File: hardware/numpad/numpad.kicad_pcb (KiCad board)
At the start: 2 copper layers, 83 x 124 mm, 116 parts, among them J1 USB_C_Receptacle_USB2.0_16P, J2 Conn_01x03, J3 Conn_01x04, Q1 BSS138, Q2 BSS138, SW1 BOOTSEL, SW2 RESET, SW3 RotaryEncoder_Switch, U1 NCP1117-3.3_SOT223, U2 USBLC6-2SC6, U3 RP2040, U4 W25Q128JVS, U5 74AHCT1G125, Y1 12MHz

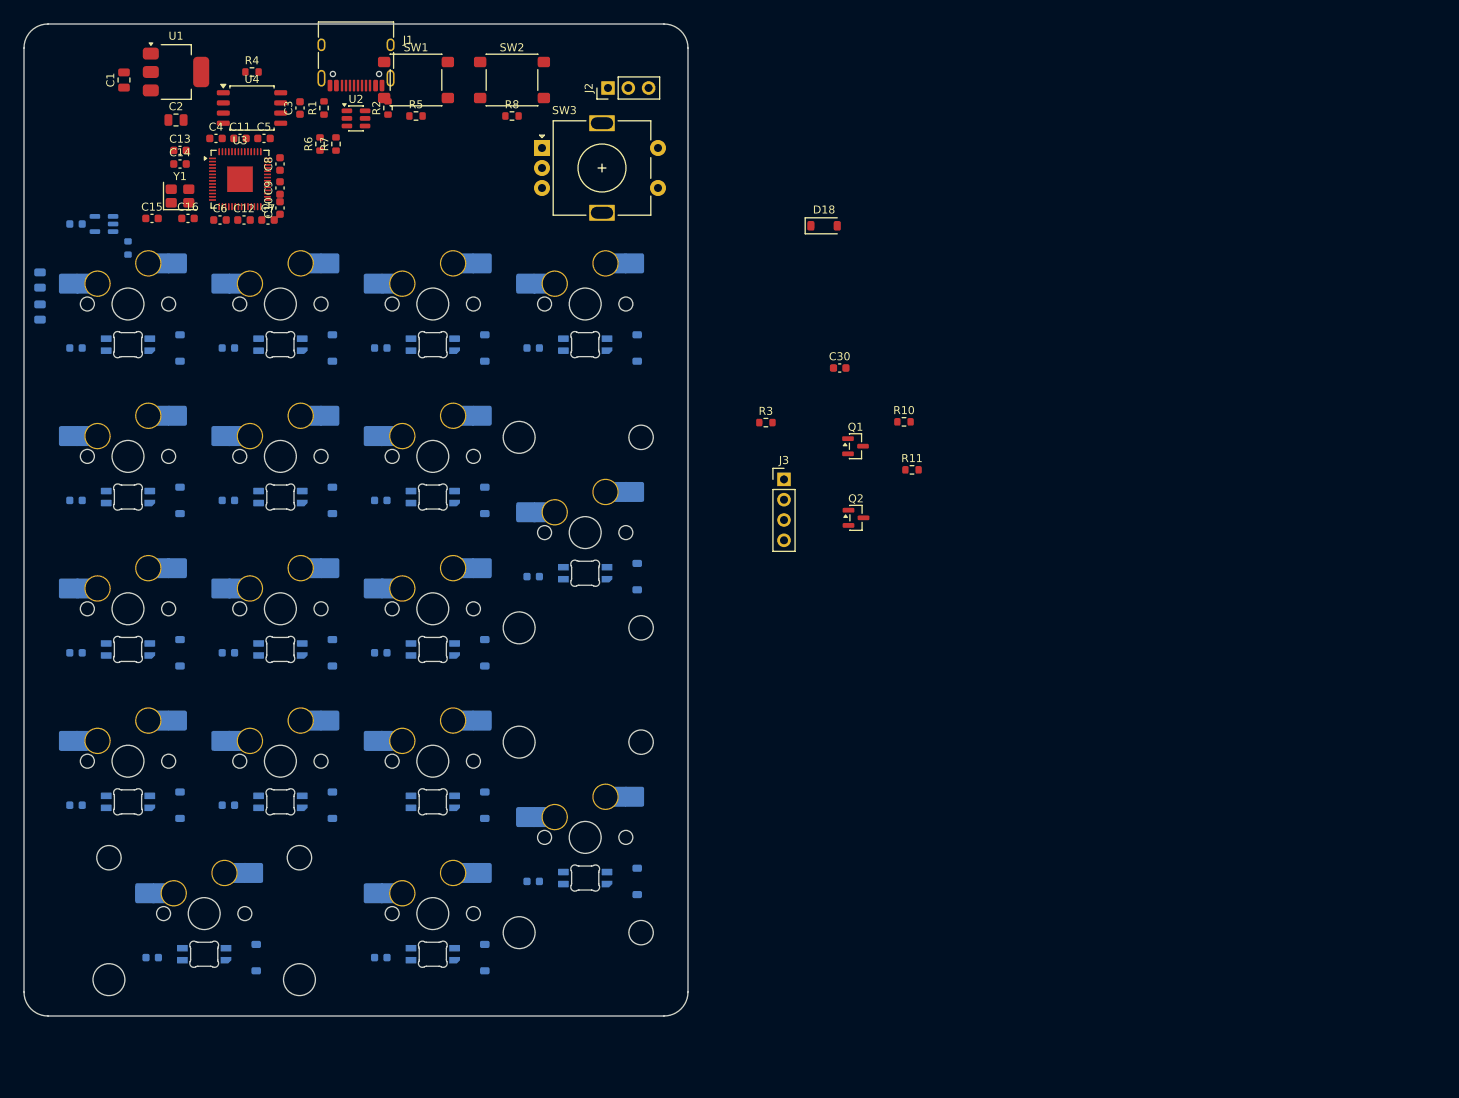
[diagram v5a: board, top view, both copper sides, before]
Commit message: placement, ground pour complete, DRC clean
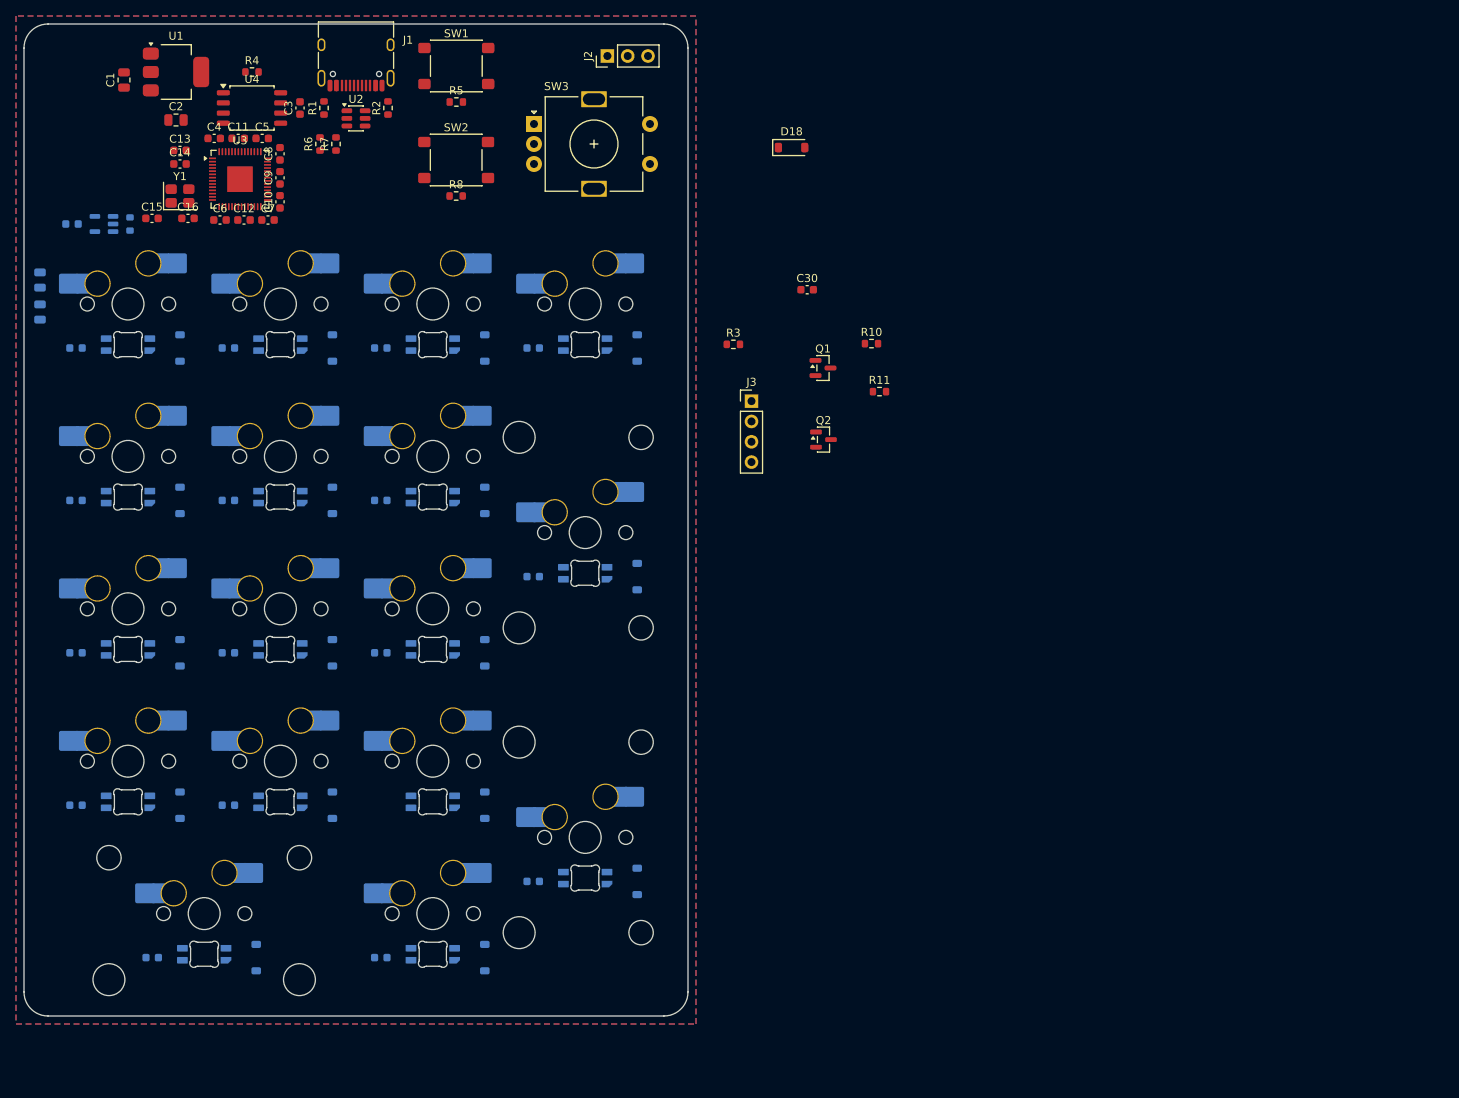
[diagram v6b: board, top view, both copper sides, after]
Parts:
- moved R8 12.2 mm to (101.0, 26.5)
- moved SW2 12.2 mm to (101.0, 22.0)
- moved C30 10.6 mm to (144.9, 38.2)
- moved D18 10.6 mm to (142.9, 20.4)
- moved J3 10.6 mm to (137.9, 52.1)
- moved Q1 10.6 mm to (146.9, 48.0)
- moved Q2 10.6 mm to (146.9, 57.0)
- moved R3 10.6 mm to (135.7, 45.0)
- moved R10 10.6 mm to (152.9, 45.0)
- moved R11 10.6 mm to (153.9, 51.0)
- moved R5 5.34 mm to (101.0, 14.8)
- moved SW1 5.34 mm to (101.0, 10.2)
- moved J2 4.00 mm to (119.9, 9.00)
- moved SW3 3.16 mm to (110.8, 17.5)
- moved R9 3.01 mm to (60.2, 30.0)
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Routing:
- added copper zone on B.Cu, net GND
- added copper zone on F.Cu, net GND
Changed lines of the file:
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@@
 		(capping no)
 		(filling no)
+		(zone_defaults)
 		(pcbplotparams
 			(layerselection 0x00000000_00000000_55555555_5755f5ff)
@@
 	(footprint "Package_TO_SOT_SMD:SOT-23"
 		(layer "F.Cu")
-		(at 151 66.73)
+		(at 146.9375 56.95)
 		(descr "SOT, 3 Pin (JEDEC TO-236 Var AB https://www.jedec.org/document_search?search_api_views_fulltext=TO-236)")
 		(tags "SOT TO_SOT_SMD")
@@
 	(footprint "Resistor_SMD:R_0603_1608Metric"
 		(layer "F.Cu")
-		(at 139.735 54.825)
+		(at 135.6725 45.045)
 		(descr "Resistor SMD 0603 (1608 Metric), square (rectangular) end terminal, IPC-7351 nominal, (Body size source: IPC-SM-782 page 72, https://www.pcb-3d.com/wordpress/wp-content/uploads/ipc-sm-782a_amendment_1_and_2.pdf)")
 		(tags "resistor")
@@
 	)
 	(footprint "Connector_PinHeader_2.54mm:PinHeader_1x03_P2.54mm_Vertical"
-		(locked yes)
 		(layer "F.Cu")
-		(at 120 13 90)
+		(at 119.92 9 90)
 		(descr "Through hole straight pin header, 1x03, 2.54mm pitch, single row")
 		(tags "Through hole pin header THT 1x03 2.54mm single row")
@@
 	(footprint "Diode_SMD:D_SOD-123"
 		(layer "F.Cu")
-		(at 147.01 30.225)
+		(at 142.9475 20.445)
 		(descr "SOD-123")
 		(tags "SOD-123")
@@
 	)
 	(footprint "Capacitor_SMD:C_0603_1608Metric"
-		(locked yes)
 		(layer "F.Cu")
-		(at 77 19.3)
+		(at 76.775 19.3)
 		(descr "Capacitor SMD 0603 (1608 Metric), square (rectangular) end terminal, IPC-7351 nominal, (Body size source: IPC-SM-782 page 76, https://www.pcb-3d.com/wordpress/wp-content/uploads/ipc-sm-782a_amendment_1_and_2.pdf)")
 		(tags "capacitor")
@@
 	)
 	(footprint "Capacitor_SMD:C_0603_1608Metric"
-		(locked yes)
 		(layer "F.Cu")
-		(at 79 22.5 90)
+		(at 79 21.225 90)
 		(descr "Capacitor SMD 0603 (1608 Metric), square (rectangular) end terminal, IPC-7351 nominal, (Body size source: IPC-SM-782 page 76, https://www.pcb-3d.com/wordpress/wp-content/uploads/ipc-sm-782a_amendment_1_and_2.pdf)")
 		(tags "capacitor")
@@
 	(footprint "Connector_PinHeader_2.54mm:PinHeader_1x04_P2.54mm_Vertical"
 		(layer "F.Cu")
-		(at 142 61.92)
+		(at 137.9375 52.14)
 		(descr "Through hole straight pin header, 1x04, 2.54mm pitch, single row")
 		(tags "Through hole pin header THT 1x04 2.54mm single row")
@@
 	)
 	(footprint "Button_Switch_SMD:SW_SPST_PTS645Sx43SMTR92"
-		(locked yes)
 		(layer "F.Cu")
-		(at 108 12)
+		(at 101.02 22)
 		(descr "Tactile switch, 6x6 mm, H4.3 mm, gullwing terminals, https://www.ckswitches.com/media/1471/pts645.pdf")
 		(tags "SPST Button Switch CK C&K")
@@
 	(footprint "Resistor_SMD:R_0603_1608Metric"
 		(layer "F.Cu")
-		(at 158 60.73)
+		(at 153.9375 50.95)
 		(descr "Resistor SMD 0603 (1608 Metric), square (rectangular) end terminal, IPC-7351 nominal, (Body size source: IPC-SM-782 page 72, https://www.pcb-3d.com/wordpress/wp-content/uploads/ipc-sm-782a_amendment_1_and_2.pdf)")
 		(tags "resistor")
@@
 	)
 	(footprint "Rotary_Encoder:RotaryEncoder_Alps_EC11E-Switch_Vertical_H20mm"
-		(locked yes)
 		(layer "F.Cu")
-		(at 111.75 20.5)
+		(at 110.75 17.5)
 		(descr "Alps rotary encoder, EC11E... with switch, vertical shaft, http://www.alps.com/prod/info/E/HTML/Encoder/Incremental/EC11/EC11E15204A3.html")
 		(tags "rotary encoder")
@@
 	)
 	(footprint "Button_Switch_SMD:SW_SPST_PTS645Sx43SMTR92"
-		(locked yes)
 		(layer "F.Cu")
-		(at 96 12)
+		(at 101.04 10.25)
 		(descr "Tactile switch, 6x6 mm, H4.3 mm, gullwing terminals, https://www.ckswitches.com/media/1471/pts645.pdf")
 		(tags "SPST Button Switch CK C&K")
@@
 	)
 	(footprint "Capacitor_SMD:C_0603_1608Metric"
-		(locked yes)
 		(layer "F.Cu")
-		(at 71 19.3)
+		(at 70.775 19.3)
 		(descr "Capacitor SMD 0603 (1608 Metric), square (rectangular) end terminal, IPC-7351 nominal, (Body size source: IPC-SM-782 page 76, https://www.pcb-3d.com/wordpress/wp-content/uploads/ipc-sm-782a_amendment_1_and_2.pdf)")
 		(tags "capacitor")
@@
 	)
 	(footprint "Resistor_SMD:R_0603_1608Metric"
-		(locked yes)
 		(layer "F.Cu")
-		(at 96 16.5)
+		(at 101.04 14.75)
 		(descr "Resistor SMD 0603 (1608 Metric), square (rectangular) end terminal, IPC-7351 nominal, (Body size source: IPC-SM-782 page 72, https://www.pcb-3d.com/wordpress/wp-content/uploads/ipc-sm-782a_amendment_1_and_2.pdf)")
 		(tags "resistor")
@@
 	)
 	(footprint "Resistor_SMD:R_0603_1608Metric"
-		(locked yes)
 		(layer "F.Cu")
-		(at 108 16.5)
+		(at 101.02 26.5)
 		(descr "Resistor SMD 0603 (1608 Metric), square (rectangular) end terminal, IPC-7351 nominal, (Body size source: IPC-SM-782 page 72, https://www.pcb-3d.com/wordpress/wp-content/uploads/ipc-sm-782a_amendment_1_and_2.pdf)")
 		(tags "resistor")
@@
 	)
 	(footprint "Capacitor_SMD:C_0603_1608Metric"
-		(locked yes)
 		(layer "F.Cu")
-		(at 79 25.5 90)
+		(at 79 24.225 90)
 		(descr "Capacitor SMD 0603 (1608 Metric), square (rectangular) end terminal, IPC-7351 nominal, (Body size source: IPC-SM-782 page 76, https://www.pcb-3d.com/wordpress/wp-content/uploads/ipc-sm-782a_amendment_1_and_2.pdf)")
 		(tags "capacitor")
@@
 	(footprint "Package_TO_SOT_SMD:SOT-23"
 		(layer "F.Cu")
-		(at 150.9375 57.78)
+		(at 146.875 48)
 		(descr "SOT, 3 Pin (JEDEC TO-236 Var AB https://www.jedec.org/document_search?search_api_views_fulltext=TO-236)")
 		(tags "SOT TO_SOT_SMD")
@@
 	)
 	(footprint "Capacitor_SMD:C_0603_1608Metric"
-		(locked yes)
 		(layer "F.Cu")
-		(at 74 19.3)
+		(at 73.775 19.3)
 		(descr "Capacitor SMD 0603 (1608 Metric), square (rectangular) end terminal, IPC-7351 nominal, (Body size source: IPC-SM-782 page 76, https://www.pcb-3d.com/wordpress/wp-content/uploads/ipc-sm-782a_amendment_1_and_2.pdf)")
 		(tags "capacitor")
@@
 	)
 	(footprint "Capacitor_SMD:C_0603_1608Metric"
-		(locked yes)
 		(layer "F.Cu")
-		(at 79 28 90)
+		(at 79 27.225 90)
 		(descr "Capacitor SMD 0603 (1608 Metric), square (rectangular) end terminal, IPC-7351 nominal, (Body size source: IPC-SM-782 page 76, https://www.pcb-3d.com/wordpress/wp-content/uploads/ipc-sm-782a_amendment_1_and_2.pdf)")
 		(tags "capacitor")
@@
 	(footprint "Capacitor_SMD:C_0603_1608Metric"
 		(layer "F.Cu")
-		(at 148.96 48)
+		(at 144.8975 38.22)
 		(descr "Capacitor SMD 0603 (1608 Metric), square (rectangular) end terminal, IPC-7351 nominal, (Body size source: IPC-SM-782 page 76, https://www.pcb-3d.com/wordpress/wp-content/uploads/ipc-sm-782a_amendment_1_and_2.pdf)")
 		(tags "capacitor")
@@
 	(footprint "Resistor_SMD:R_0603_1608Metric"
 		(layer "F.Cu")
-		(at 157 54.73)
+		(at 152.9375 44.95)
 		(descr "Resistor SMD 0603 (1608 Metric), square (rectangular) end terminal, IPC-7351 nominal, (Body size source: IPC-SM-782 page 72, https://www.pcb-3d.com/wordpress/wp-content/uploads/ipc-sm-782a_amendment_1_and_2.pdf)")
 		(tags "resistor")
@@
 	)
 	(footprint "Capacitor_SMD:C_0603_1608Metric"
-		(locked yes)
 		(layer "B.Cu")
-		(at 53.5 30 180)
+		(at 53 30 180)
 		(descr "Capacitor SMD 0603 (1608 Metric), square (rectangular) end terminal, IPC-7351 nominal, (Body size source: IPC-SM-782 page 76, https://www.pcb-3d.com/wordpress/wp-content/uploads/ipc-sm-782a_amendment_1_and_2.pdf)")
 		(tags "capacitor")
@@
 	)
 	(footprint "Resistor_SMD:R_0603_1608Metric"
-		(locked yes)
 		(layer "B.Cu")
-		(at 60 33 90)
+		(at 60.25 30 90)
 		(descr "Resistor SMD 0603 (1608 Metric), square (rectangular) end terminal, IPC-7351 nominal, (Body size source: IPC-SM-782 page 72, https://www.pcb-3d.com/wordpress/wp-content/uploads/ipc-sm-782a_amendment_1_and_2.pdf)")
 		(tags "resistor")
@@
 		(layer "Edge.Cuts")
 	)
+	(zone
+		(net "GND")
+		(layers "F.Cu" "B.Cu")
+		(hatch edge 0.5)
+		(connect_pads
+			(clearance 0.5)
+		)
+		(min_thickness 0.25)
+		(fill yes
+			(thermal_gap 0.5)
+			(thermal_bridge_width 0.5)
+			(island_removal_mode 0)
+		)
+		(polygon
+			(pts
+				(xy 131 4) (xy 46 4) (xy 46 130) (xy 131 130)
+			)
+		)
+	)
 	(embedded_fonts no)

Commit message: pours and final placement
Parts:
- C30, Q1, Q2, R10, R11: moved to B.Cu
- moved J3 94.3 mm to (50.0, 18.0)
- moved J2 69.9 mm to (50.0, 8.46), turned to 0 degrees
- moved R10 62.3 mm to (95.0, 22.0), turned to 90 degrees
- moved Q2 55.4 mm to (104.0, 22.0), turned to 180 degrees
- moved Q1 55.4 mm to (98.0, 22.0), turned to 180 degrees
- moved R11 55.1 mm to (107.0, 22.0), turned to 90 degrees
- moved C30 52.5 mm to (94.0, 25.5), turned to 180 degrees
- moved R3 40.8 mm to (107.0, 16.0), turned to 90 degrees
- moved D18 22.0 mm to (121.5, 25.2)
- moved SW3 16.3 mm to (124.0, 8.00), turned to -90 degrees

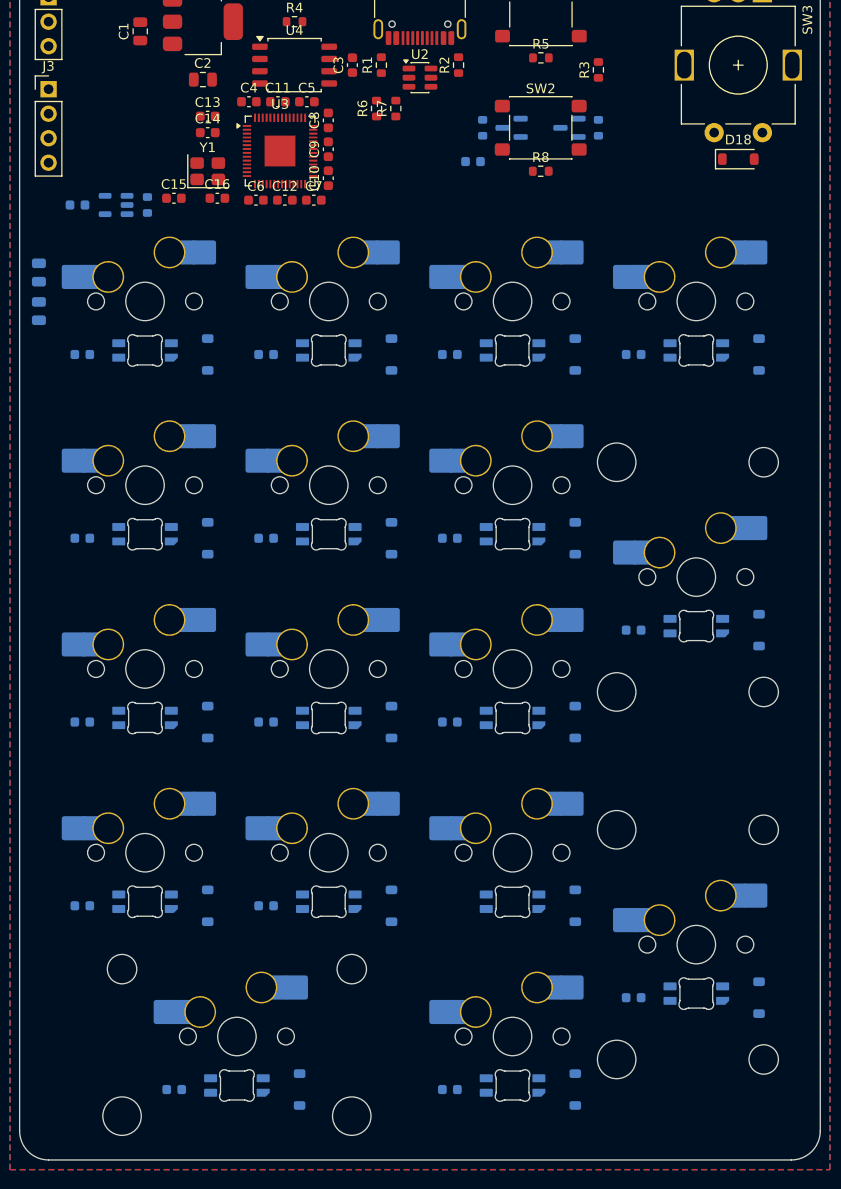
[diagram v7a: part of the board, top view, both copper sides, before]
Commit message: component repositioning, more routing
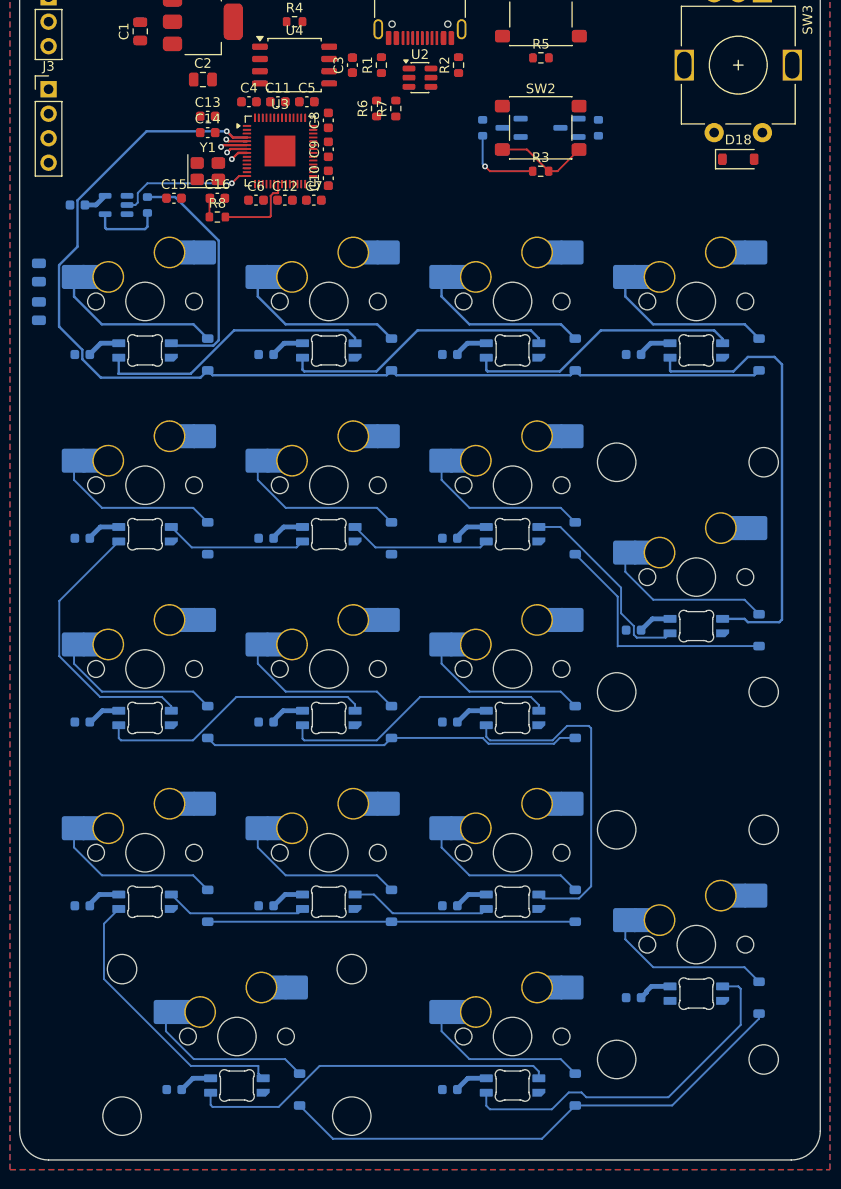
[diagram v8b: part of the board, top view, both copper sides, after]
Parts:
- moved C30 77.2 mm to (91.6, 102.7)
- moved R8 33.9 mm to (67.5, 31.2)
- moved R3 12.1 mm to (101.0, 26.5), turned to 0 degrees
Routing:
- net /02_mcu/ROW0: track 0.00 -> 111.5 mm, vias 0 -> 1
- net +5V: track 0.00 -> 62.5 mm
- net /02_mcu/ROW4: track 0.00 -> 56.6 mm, vias 0 -> 1
- net Net-(LED4-DOUT): track 0.00 -> 46.8 mm
- net /02_mcu/ROW2: track 0.00 -> 42.0 mm, vias 0 -> 1
- net /02_mcu/ROW3: track 0.00 -> 40.3 mm, vias 0 -> 1
- net Net-(LED15-DOUT): track 0.00 -> 38.1 mm
- net Net-(LED16-DOUT): track 0.00 -> 37.6 mm
- net Net-(LED11-DOUT): track 0.00 -> 35.4 mm
- net Net-(LED14-DOUT): track 0.00 -> 29.1 mm
- net Net-(LED1-DOUT): track 0.00 -> 28.9 mm
- net Net-(LED10-DIN): track 0.00 -> 28.8 mm
- net Net-(LED10-DOUT): track 0.00 -> 28.8 mm
- net Net-(LED8-DOUT): track 0.00 -> 28.7 mm
- net Net-(LED3-DOUT): track 0.00 -> 28.4 mm
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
